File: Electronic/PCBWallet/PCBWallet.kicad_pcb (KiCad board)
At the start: 2 copper layers, 122 x 84 mm, 1 part

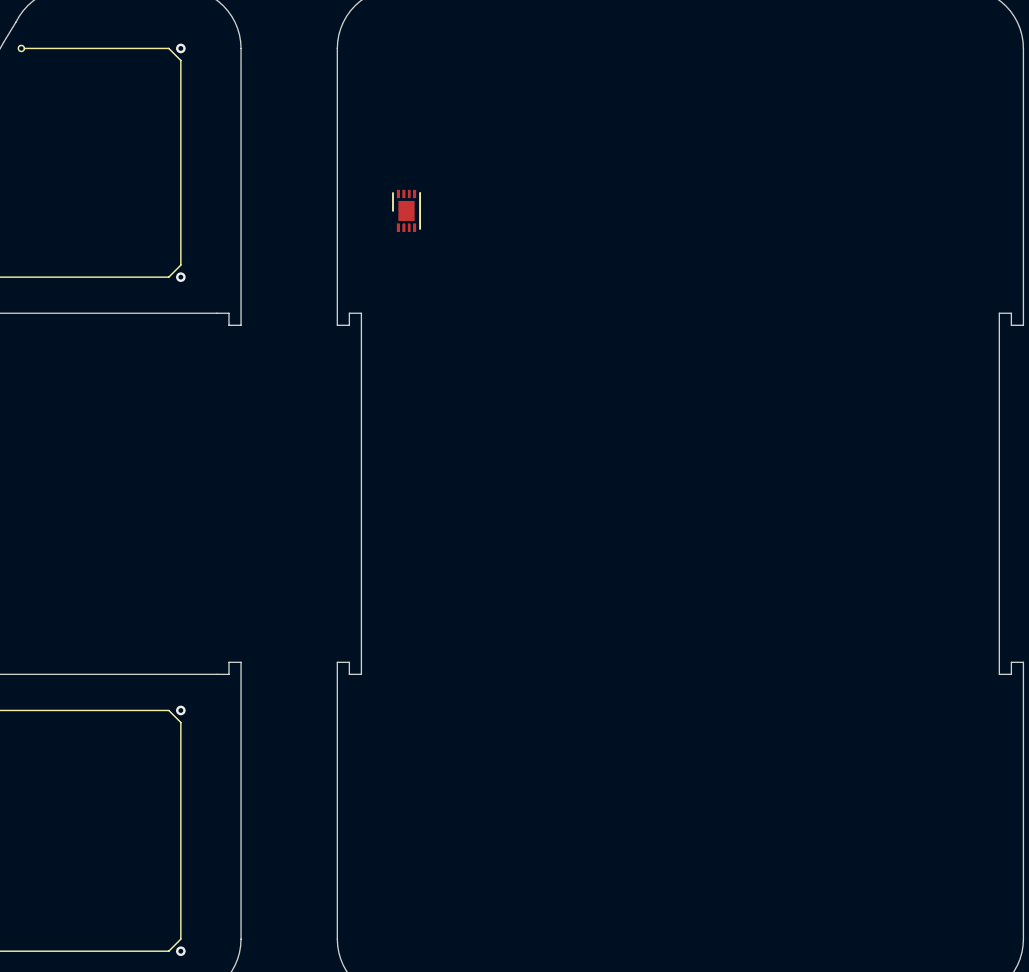
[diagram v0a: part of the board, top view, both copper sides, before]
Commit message: create pcbwallet schematic -  quite simple
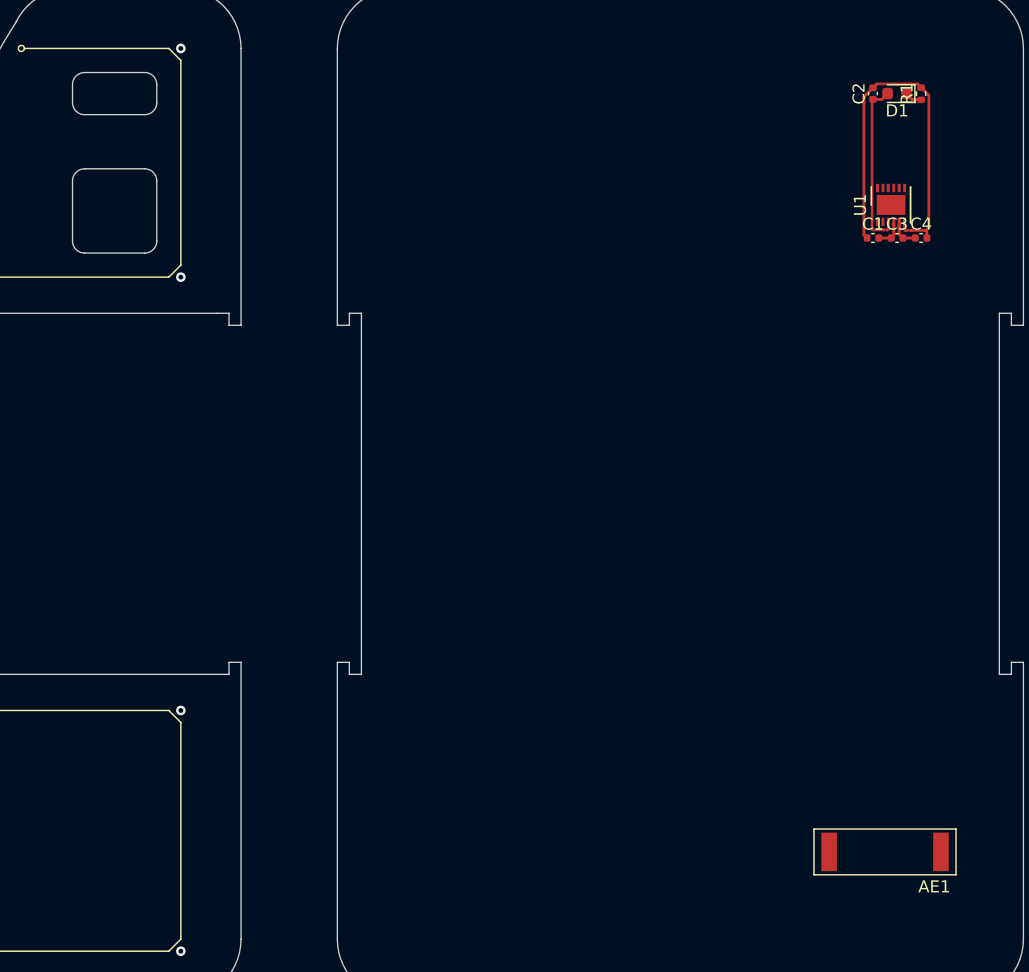
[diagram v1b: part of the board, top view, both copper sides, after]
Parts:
- removed REF**: DFN-8-1EP_3x2mm_P0.45mm_EP1.66x1.36mm, Package_DFN_QFN:DFN-8-1EP_3x2mm_P0.45mm_EP1.66x1.36mm
- added AE1: Antenna_Loop, RF_Antenna:Coilcraft_MA5532-AE_RFID, F.Cu at (210.5, 121.8)
- added C1: 50pF, Capacitor_SMD:C_0402_1005Metric, F.Cu at (209.5, 70.8)
- added C2: 50pF, Capacitor_SMD:C_0402_1005Metric, F.Cu at (209.5, 58.8)
- added C3: 50pF, Capacitor_SMD:C_0402_1005Metric, F.Cu at (211.5, 70.8)
- added C4: 50pF, Capacitor_SMD:C_0402_1005Metric, F.Cu at (213.5, 70.8)
- added D1: LED, LED_SMD:LED_0603_1608Metric, F.Cu at (211.5, 58.8)
- added R1: 220R, Resistor_SMD:R_0402_1005Metric, F.Cu at (213.5, 58.8)
- added U1: NFCTag_ST25DV, Package_DFN_QFN:DFN-12-1EP_3x3mm_P0.45mm_EP1.66x2.38mm, F.Cu at (211.0, 68.0)
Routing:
- net GND: track 0.00 -> 32.7 mm
- net Net-(C2-Pad1): track 0.00 -> 14.2 mm
- net Net-(AE1-Pad1): track 0.00 -> 2.52 mm
- net Net-(AE1-Pad2): track 0.00 -> 2.47 mm
- net Net-(D1-Pad1): track 0.00 -> 1.43 mm
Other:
- outline, holes or cut-outs redrawn

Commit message: add pcb design
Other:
- board text added: "01101011 01101001 01101100 01101001 01100001 01101110"
- board text added: "01101011 01101100 01100101 01110000 01110000 01100101 01110010"

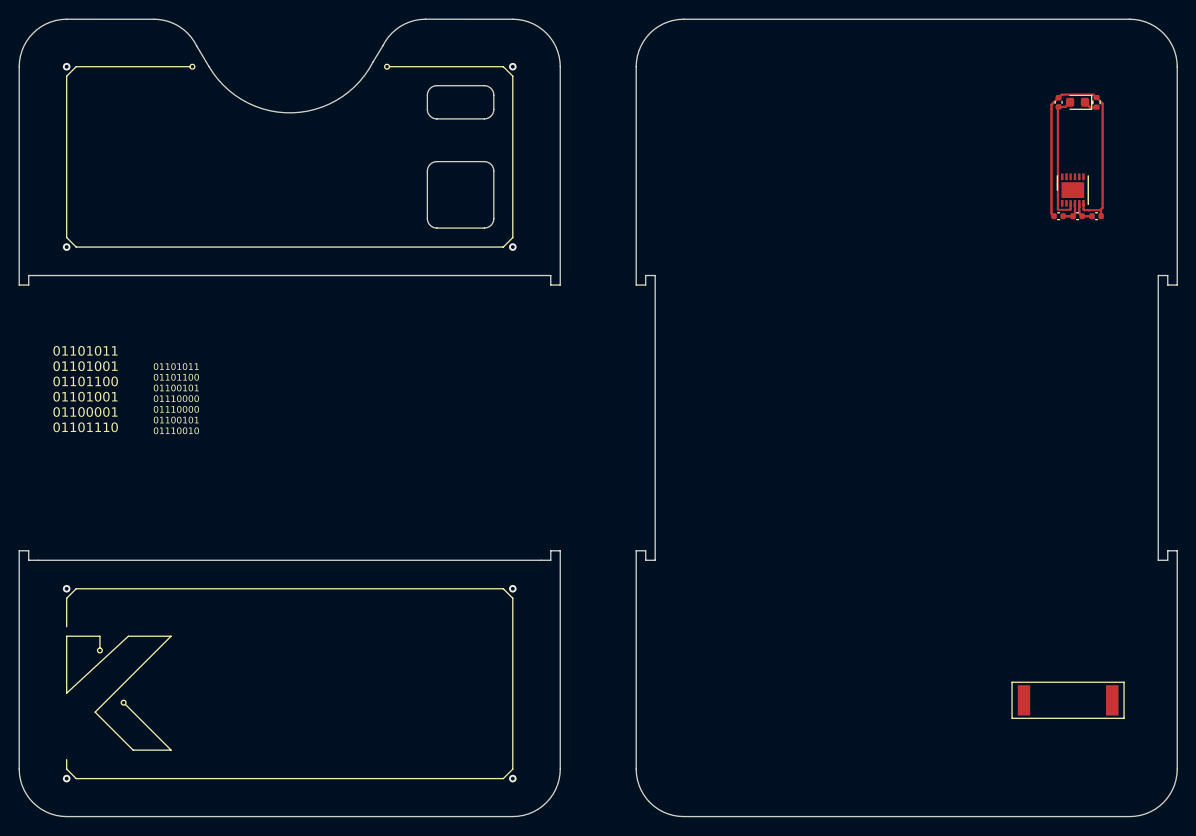
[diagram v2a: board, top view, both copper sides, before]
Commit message: add nfc antenna to layout
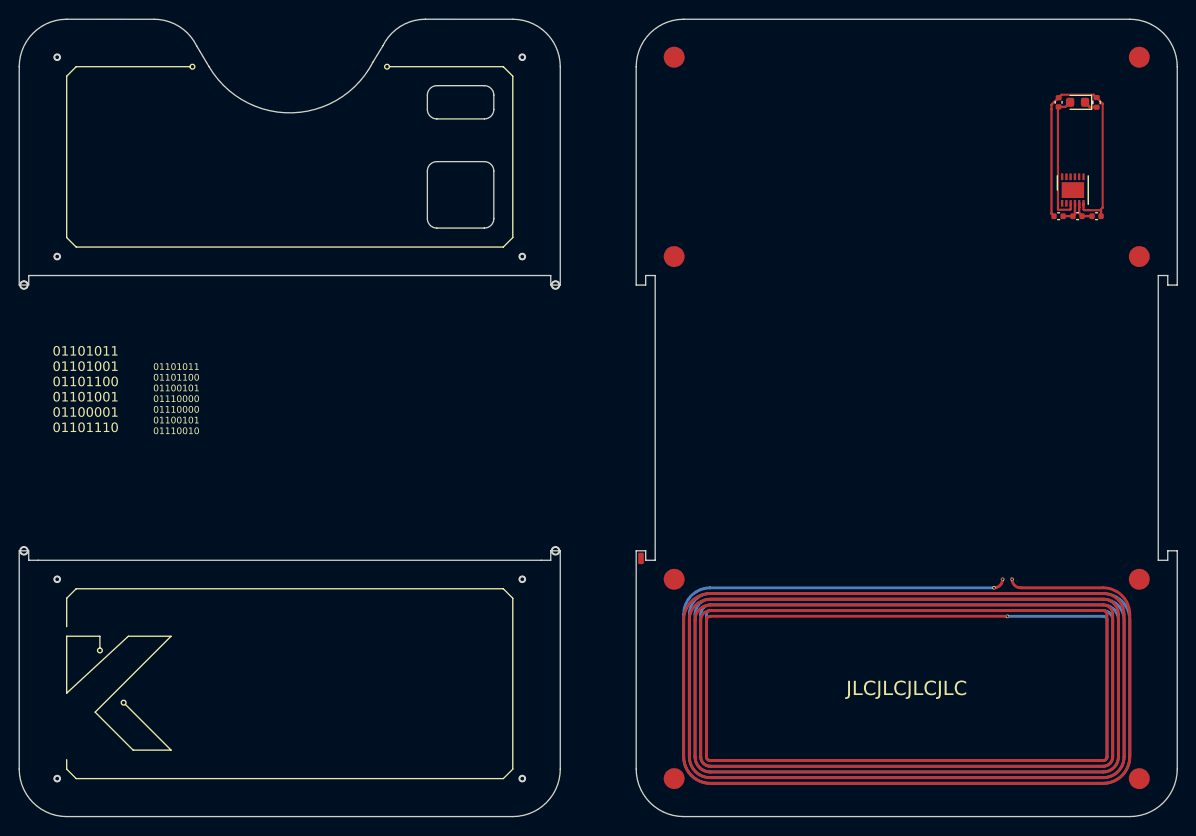
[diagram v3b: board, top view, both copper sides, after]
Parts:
- AE1: footprint RF_Antenna:Coilcraft_MA5532-AE_RFID -> Spyra_Antenna:NFC_2Layer_4.8uH_47x20
- moved AE1 17.0 mm to (193.5, 120.5), turned to 0 degrees
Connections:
- U1 pad 1: Net-(U1-Pad1) -> unconnected-(U1-Pad1)
- U1 pad 10: Net-(U1-Pad10) -> unconnected-(U1-Pad10)
- U1 pad 12: Net-(U1-Pad12) -> unconnected-(U1-Pad12)
- U1 pad 2: Net-(U1-Pad2) -> unconnected-(U1-Pad2)
- U1 pad 7: Net-(U1-Pad7) -> unconnected-(U1-Pad7)
- U1 pad 8: Net-(U1-Pad8) -> unconnected-(U1-Pad8)
- U1 pad 9: Net-(U1-Pad9) -> unconnected-(U1-Pad9)
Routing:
- net (no net): vias 8 -> 12
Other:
- net class Default removed
- board text added: "JLCJLCJLCJLC"
- board text added: "PCB WALLET"

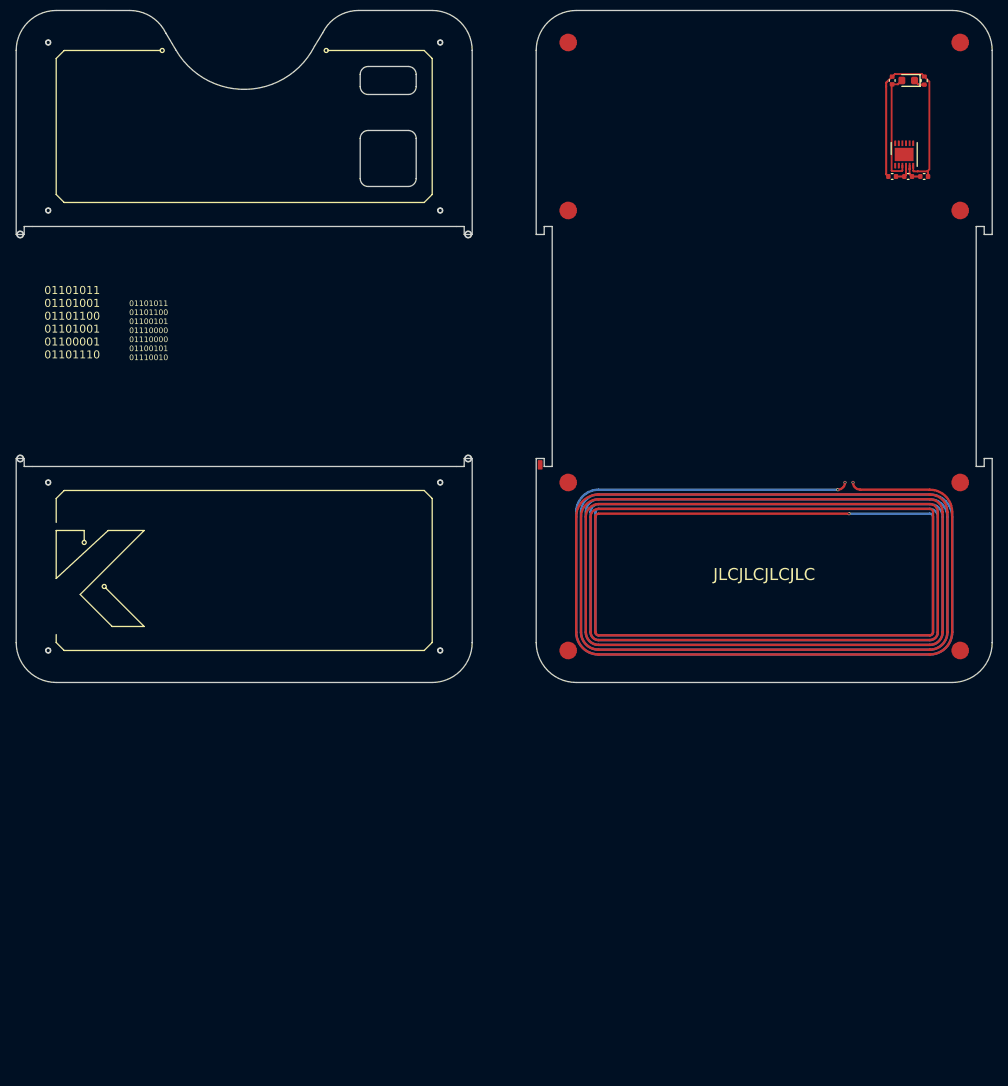
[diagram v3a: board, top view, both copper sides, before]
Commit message: add generative art to pcb layout
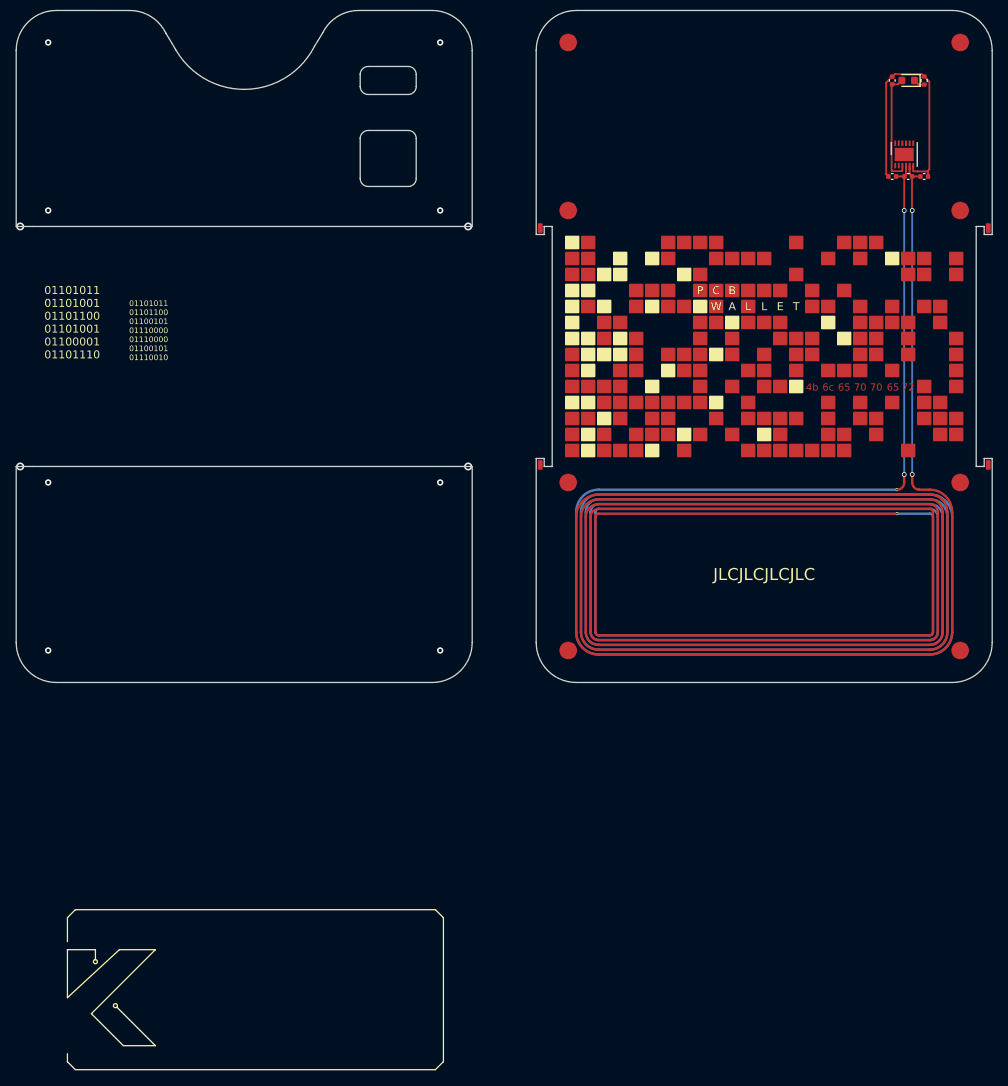
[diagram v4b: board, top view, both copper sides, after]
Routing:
- net Net-(AE1-Pad1): track 2.52 -> 40.4 mm, vias 0 -> 2
- net Net-(AE1-Pad2): track 2.47 -> 40.3 mm, vias 0 -> 2
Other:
- outline, holes or cut-outs redrawn
- board text added: "4b"
- board text added: "65"
- board text added: "6c"
- board text added: "70"
- board text added: "72"
- board text added: "A"
- board text added: "B"
- board text added: "C"
- board text added: "E"
- board text added: "L"
- board text added: "P"
- board text added: "T"
- board text added: "W"
